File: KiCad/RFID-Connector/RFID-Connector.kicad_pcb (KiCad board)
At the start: 2 copper layers, 80 x 55.5 mm, 10 parts, among them J1 +5V power supply, J2 3V3 RX TX GND, SW1 SW_RESET_TAG_IDs, U1 ESP32-DEVKITC

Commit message: updated PCB
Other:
- board text added: "RFID-Connector PCB 1.0"
- board text removed: "RaceBox PCB 1.0"
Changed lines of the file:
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@@
   (gr_line (start 88 75.5) (end 88 20) (layer "Edge.Cuts") (width 0.1))
   (gr_circle (center 163 70.5) (end 164.5 70.5) (layer "Edge.Cuts") (width 0.1) (fill none))
-  (gr_text "RaceBox\nPCB 1.0" (at 105.45 32.725) (layer "F.SilkS")
+  (gr_text "RFID-Connector\nPCB 1.0" (at 107.95 35.56) (layer "F.SilkS")
     (effects (font (size 3 3) (thickness 0.75)))
   )

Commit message: updated pcb
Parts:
- moved J1 5.00 mm to (94.6, 50.9)
- moved J2 5.00 mm to (119.4, 66.1)
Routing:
- net Net-(J2-Pad2): track 19.9 -> 13.1 mm
- net Net-(J2-Pad3): track 19.9 -> 13.1 mm
- net Net-(J1-Pad2): track 145.8 -> 140.4 mm
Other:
- board size 80 x 55.5 mm -> 90 x 55.5 mm
- board text added: "120Ω"
- board text added: "BU"
- board text added: "RD"
- board text added: "YE"
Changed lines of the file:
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@@
   )
   (footprint "Connector_PinHeader_2.54mm:PinHeader_1x06_P2.54mm_Vertical" (layer "F.Cu")
-    (at 94.615 55.88 180)
+    (at 94.615 50.88 180)
     (descr "Through hole straight pin header, 1x06, 2.54mm pitch, single row")
     (tags "Through hole pin header THT 1x06 2.54mm single row")
@@
   )
   (footprint "Connector_PinHeader_2.54mm:PinHeader_1x04_P2.54mm_Vertical" (layer "F.Cu")
-    (at 119.38 71.12 180)
+    (at 119.38 66.12 180)
     (descr "Through hole straight pin header, 1x04, 2.54mm pitch, single row")
     (tags "Through hole pin header THT 1x04 2.54mm single row")
@@
   (gr_line (start 88.25 75.5) (end 121.25 75.5) (layer "Dwgs.User") (width 0.2))
   (gr_line (start 121.25 75.5) (end 121.25 20.5) (layer "Dwgs.User") (width 0.2))
-  (gr_circle (center 93 25) (end 94.5 25) (layer "Edge.Cuts") (width 0.1) (fill none))
-  (gr_circle (center 93 70.5) (end 94.5 70.5) (layer "Edge.Cuts") (width 0.1) (fill none))
+  (gr_circle (center 83 25) (end 84.5 25) (layer "Edge.Cuts") (width 0.1) (fill none))
+  (gr_circle (center 83 70.5) (end 84.5 70.5) (layer "Edge.Cuts") (width 0.1) (fill none))
   (gr_circle (center 163 25) (end 164.5 25) (layer "Edge.Cuts") (width 0.1) (fill none))
-  (gr_line (start 168 20) (end 88 20) (layer "Edge.Cuts") (width 0.1))
-  (gr_line (start 168 75.5) (end 88 75.5) (layer "Edge.Cuts") (width 0.1))
+  (gr_line (start 168 20) (end 78 20) (layer "Edge.Cuts") (width 0.1))
+  (gr_line (start 168 75.5) (end 78 75.5) (layer "Edge.Cuts") (width 0.1))
   (gr_line (start 168 75.5) (end 168 20) (layer "Edge.Cuts") (width 0.1))
-  (gr_line (start 88 75.5) (end 88 20) (layer "Edge.Cuts") (width 0.1))
+  (gr_line (start 78 75.5) (end 78 20) (layer "Edge.Cuts") (width 0.1))
   (gr_circle (center 163 70.5) (end 164.5 70.5) (layer "Edge.Cuts") (width 0.1) (fill none))
-  (gr_text "RFID-Connector\nPCB 1.0" (at 107.95 35.56) (layer "F.SilkS")
+  (gr_text "RFID-Connector\nPCB 1.0" (at 106.045 29.21) (layer "F.SilkS")
     (effects (font (size 3 3) (thickness 0.75)))
   )
-  (gr_text "R200" (at 105.41 59.69) (layer "F.SilkS")
+  (gr_text "RD" (at 133.35 66.04) (layer "F.SilkS")
+    (effects (font (size 1 1) (thickness 0.15)))
+  )
+  (gr_text "R200" (at 105.41 50.8) (layer "F.SilkS")
     (effects (font (size 1.8 1.8) (thickness 0.3)))
+  )
+  (gr_text "BU" (at 133.35 55.88) (layer "F.SilkS")
+    (effects (font (size 1 1) (thickness 0.15)))
   )
   (gr_text "ESP32\nDEVKIT V4" (at 146.05 71.12) (layer "F.SilkS")
     (effects (font (size 1.8 1.8) (thickness 0.3)))
+  )
+  (gr_text "YE" (at 133.35 45.72) (layer "F.SilkS")
+    (effects (font (size 1 1) (thickness 0.15)))
+  )
+  (gr_text "120Ω" (at 148.59 50.8) (layer "F.SilkS")
+    (effects (font (size 1 1) (thickness 0.15)))
   )
   (segment (start 138.43 44.45) (end 138.43 45.72) (width 1.5) (layer "B.Cu") (net 1))
@@
   (segment (start 144.78 48.26) (end 140.97 52.07) (width 1.5) (layer "B.Cu") (net 4))
   (segment (start 140.97 52.07) (end 140.97 63.5) (width 1.5) (layer "B.Cu") (net 4))
+  (segment (start 101.6 43.815) (end 101.6 45.085) (width 1.5) (layer "F.Cu") (net 6))
   (segment (start 160.02 25.4) (end 157.48 22.86) (width 1.5) (layer "F.Cu") (net 6))
-  (segment (start 99.06 53.34) (end 94.615 53.34) (width 1.5) (layer "F.Cu") (net 6))
   (segment (start 104.14 22.86) (end 101.6 25.4) (width 1.5) (layer "F.Cu") (net 6))
   (segment (start 157.48 22.86) (end 104.14 22.86) (width 1.5) (layer "F.Cu") (net 6))
-  (segment (start 101.6 25.4) (end 101.6 50.8) (width 1.5) (layer "F.Cu") (net 6))
-  (segment (start 101.6 50.8) (end 99.06 53.34) (width 1.5) (layer "F.Cu") (net 6))
+  (segment (start 101.6 25.4) (end 101.6 43.815) (width 1.5) (layer "F.Cu") (net 6))
   (segment (start 157.47 73.67) (end 160.02 71.12) (width 1.5) (layer "F.Cu") (net 6))
+  (segment (start 101.6 45.085) (end 98.345 48.34) (width 1.5) (layer "F.Cu") (net 6))
   (segment (start 160.02 71.12) (end 160.02 25.4) (width 1.5) (layer "F.Cu") (net 6))
+  (segment (start 98.345 48.34) (end 94.615 48.34) (width 1.5) (layer "F.Cu") (net 6))
   (segment (start 154.94 73.67) (end 157.47 73.67) (width 1.5) (layer "F.Cu") (net 6))
-  (segment (start 127 64.77) (end 123.19 68.58) (width 1.5) (layer "F.Cu") (net 12))
-  (segment (start 127 57.15) (end 127 64.77) (width 1.5) (layer "F.Cu") (net 12))
+  (segment (start 127 59.69) (end 123.19 63.5) (width 1.5) (layer "F.Cu") (net 12))
+  (segment (start 123.19 63.5) (end 121.08 63.5) (width 1.5) (layer "F.Cu") (net 12))
   (segment (start 129.54 55.89) (end 128.26 55.89) (width 1.5) (layer "F.Cu") (net 12))
-  (segment (start 123.19 68.58) (end 119.38 68.58) (width 1.5) (layer "F.Cu") (net 12))
   (segment (start 128.26 55.89) (end 127 57.15) (width 1.5) (layer "F.Cu") (net 12))
+  (segment (start 127 57.15) (end 127 59.69) (width 1.5) (layer "F.Cu") (net 12))
+  (segment (start 124.46 55.88) (end 124.46 58.42) (width 1.5) (layer "F.Cu") (net 13))
+  (segment (start 121.84 61.04) (end 121.08 61.04) (width 1.5) (layer "F.Cu") (net 13))
   (segment (start 129.54 53.35) (end 126.99 53.35) (width 1.5) (layer "F.Cu") (net 13))
-  (segment (start 124.46 55.88) (end 124.46 63.5) (width 1.5) (layer "F.Cu") (net 13))
-  (segment (start 124.46 63.5) (end 121.92 66.04) (width 1.5) (layer "F.Cu") (net 13))
   (segment (start 126.99 53.35) (end 124.46 55.88) (width 1.5) (layer "F.Cu") (net 13))
-  (segment (start 121.92 66.04) (end 119.38 66.04) (width 1.5) (layer "F.Cu") (net 13))
+  (segment (start 124.46 58.42) (end 121.84 61.04) (width 1.5) (layer "F.Cu") (net 13))
   (segment (start 119.38 63.5) (end 119.38 30.48) (width 1.5) (layer "F.Cu") (net 14))
   (segment (start 121.91 27.95) (end 129.54 27.95) (width 1.5) (layer "F.Cu") (net 14))

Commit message: fixed pcb
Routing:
- net Net-(J2-Pad4): track 55.2 -> 50.2 mm
- net Net-(J2-Pad2): track 13.1 -> 14.8 mm
- net Net-(J2-Pad3): track 13.1 -> 14.8 mm
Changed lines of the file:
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@@
   (segment (start 98.345 48.34) (end 94.615 48.34) (width 1.5) (layer "F.Cu") (net 6))
   (segment (start 154.94 73.67) (end 157.47 73.67) (width 1.5) (layer "F.Cu") (net 6))
-  (segment (start 127 59.69) (end 123.19 63.5) (width 1.5) (layer "F.Cu") (net 12))
-  (segment (start 123.19 63.5) (end 121.08 63.5) (width 1.5) (layer "F.Cu") (net 12))
   (segment (start 129.54 55.89) (end 128.26 55.89) (width 1.5) (layer "F.Cu") (net 12))
+  (segment (start 127 57.15) (end 127 59.69) (width 1.5) (layer "F.Cu") (net 12))
+  (segment (start 123.11 63.58) (end 119.38 63.58) (width 1.5) (layer "F.Cu") (net 12))
+  (segment (start 127 59.69) (end 123.11 63.58) (width 1.5) (layer "F.Cu") (net 12))
   (segment (start 128.26 55.89) (end 127 57.15) (width 1.5) (layer "F.Cu") (net 12))
-  (segment (start 127 57.15) (end 127 59.69) (width 1.5) (layer "F.Cu") (net 12))
+  (segment (start 121.84 61.04) (end 119.38 61.04) (width 1.5) (layer "F.Cu") (net 13))
+  (segment (start 124.46 58.42) (end 121.84 61.04) (width 1.5) (layer "F.Cu") (net 13))
   (segment (start 124.46 55.88) (end 124.46 58.42) (width 1.5) (layer "F.Cu") (net 13))
-  (segment (start 121.84 61.04) (end 121.08 61.04) (width 1.5) (layer "F.Cu") (net 13))
   (segment (start 129.54 53.35) (end 126.99 53.35) (width 1.5) (layer "F.Cu") (net 13))
   (segment (start 126.99 53.35) (end 124.46 55.88) (width 1.5) (layer "F.Cu") (net 13))
-  (segment (start 124.46 58.42) (end 121.84 61.04) (width 1.5) (layer "F.Cu") (net 13))
-  (segment (start 119.38 63.5) (end 119.38 30.48) (width 1.5) (layer "F.Cu") (net 14))
   (segment (start 121.91 27.95) (end 129.54 27.95) (width 1.5) (layer "F.Cu") (net 14))
+  (segment (start 119.38 58.5) (end 119.38 30.48) (width 1.5) (layer "F.Cu") (net 14))
   (segment (start 119.38 30.48) (end 121.91 27.95) (width 1.5) (layer "F.Cu") (net 14))
   (segment (start 133.91 28.23) (end 140.41 28.23) (width 1.5) (layer "B.Cu") (net 14))

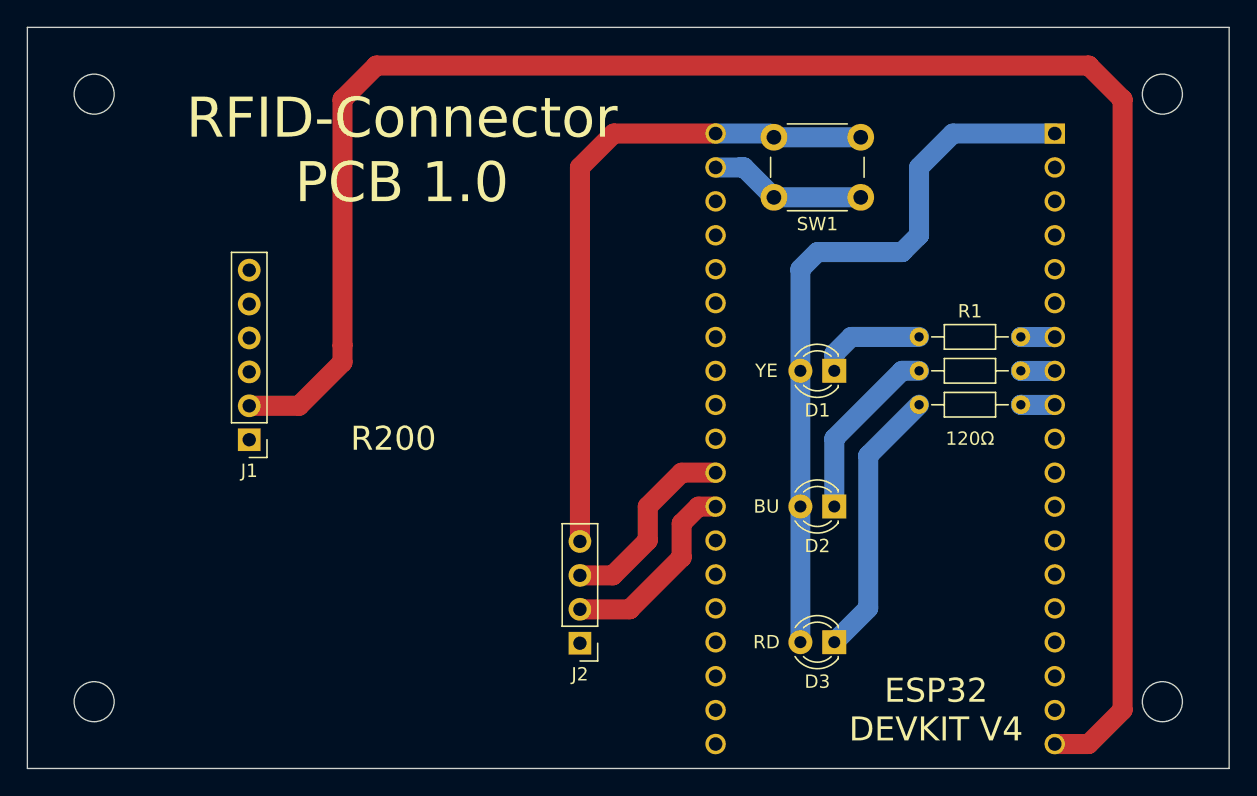
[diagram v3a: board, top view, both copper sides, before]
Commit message: added power connector to pcb
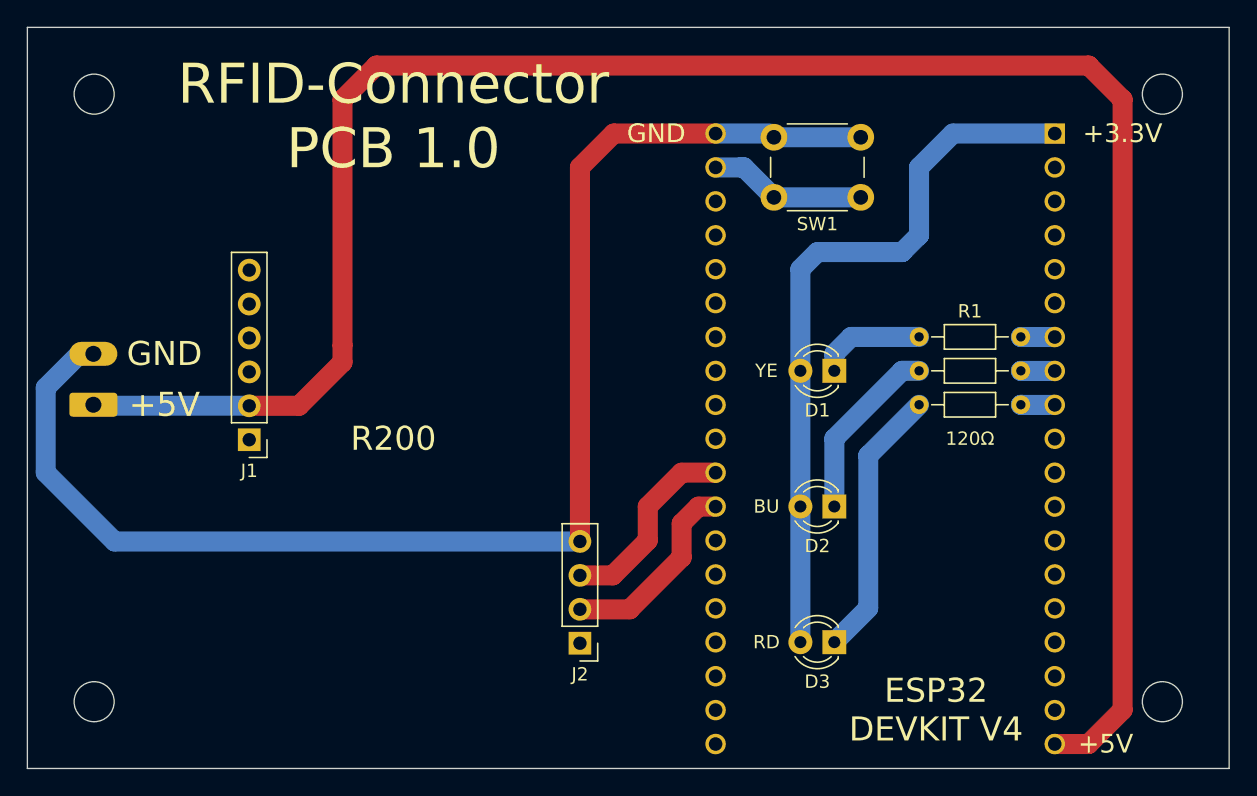
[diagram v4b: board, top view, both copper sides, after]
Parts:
- added J3: Conn_01x02, Connector_Phoenix_MC:PhoenixContact_MC_1,5_2-G-3.81_1x02_P3.81mm_Horizontal, B.Cu at (82.9, 48.3)
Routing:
- net Net-(J2-Pad4): track 50.2 -> 103.3 mm
- net Net-(J1-Pad2): track 140.4 -> 152.0 mm
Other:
- board text added: "+3.3V"
- board text added: "+5V"
- board text added: "GND"
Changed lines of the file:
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@@
     (descr "LED, diameter 3.0mm, 2 pins")
     (tags "LED diameter 3.0mm 2 pins")
-    (property "Sheetfile" "RaceBox.kicad_sch")
+    (property "Sheetfile" "RFID-Connector.kicad_sch")
     (property "Sheetname" "")
     (attr through_hole)
@@
     (descr "Resistor, Axial_DIN0204 series, Axial, Horizontal, pin pitch=7.62mm, 0.167W, length*diameter=3.6*1.6mm^2, http://cdn-reichelt.de/documents/datenblatt/B400/1_4W%23YAG.pdf")
     (tags "Resistor Axial_DIN0204 series Axial Horizontal pin pitch 7.62mm 0.167W length 3.6mm diameter 1.6mm")
-    (property "Sheetfile" "RaceBox.kicad_sch")
+    (property "Sheetfile" "RFID-Connector.kicad_sch")
     (property "Sheetname" "")
     (attr through_hole)
@@
     (descr "https://www.omron.com/ecb/products/pdf/en-b3f.pdf")
     (tags "tact sw push 6mm")
-    (property "Sheetfile" "RaceBox.kicad_sch")
+    (property "Sheetfile" "RFID-Connector.kicad_sch")
     (property "Sheetname" "")
     (attr through_hole)
@@
     (descr "LED, diameter 3.0mm, 2 pins")
     (tags "LED diameter 3.0mm 2 pins")
-    (property "Sheetfile" "RaceBox.kicad_sch")
+    (property "Sheetfile" "RFID-Connector.kicad_sch")
     (property "Sheetname" "")
     (attr through_hole)
@@
     (descr "Through hole straight pin header, 1x06, 2.54mm pitch, single row")
     (tags "Through hole pin header THT 1x06 2.54mm single row")
-    (property "Sheetfile" "RaceBox.kicad_sch")
+    (property "Sheetfile" "RFID-Connector.kicad_sch")
     (property "Sheetname" "")
     (attr through_hole)
@@
     (descr "Resistor, Axial_DIN0204 series, Axial, Horizontal, pin pitch=7.62mm, 0.167W, length*diameter=3.6*1.6mm^2, http://cdn-reichelt.de/documents/datenblatt/B400/1_4W%23YAG.pdf")
     (tags "Resistor Axial_DIN0204 series Axial Horizontal pin pitch 7.62mm 0.167W length 3.6mm diameter 1.6mm")
-    (property "Sheetfile" "RaceBox.kicad_sch")
+    (property "Sheetfile" "RFID-Connector.kicad_sch")
     (property "Sheetname" "")
     (attr through_hole)
@@
     (descr "Resistor, Axial_DIN0204 series, Axial, Horizontal, pin pitch=7.62mm, 0.167W, length*diameter=3.6*1.6mm^2, http://cdn-reichelt.de/documents/datenblatt/B400/1_4W%23YAG.pdf")
     (tags "Resistor Axial_DIN0204 series Axial Horizontal pin pitch 7.62mm 0.167W length 3.6mm diameter 1.6mm")
-    (property "Sheetfile" "RaceBox.kicad_sch")
+    (property "Sheetfile" "RFID-Connector.kicad_sch")
     (property "Sheetname" "")
     (attr through_hole)
@@
     (descr "LED, diameter 3.0mm, 2 pins")
     (tags "LED diameter 3.0mm 2 pins")
-    (property "Sheetfile" "RaceBox.kicad_sch")
+    (property "Sheetfile" "RFID-Connector.kicad_sch")
     (property "Sheetname" "")
     (attr through_hole)
@@
     (descr "Through hole straight pin header, 1x04, 2.54mm pitch, single row")
     (tags "Through hole pin header THT 1x04 2.54mm single row")
-    (property "Sheetfile" "RaceBox.kicad_sch")
+    (property "Sheetfile" "RFID-Connector.kicad_sch")
     (property "Sheetname" "")
     (attr through_hole)
@@
     (property "Price" "None")
     (property "STANDARD" "Manufacturer Recommendations")
-    (property "Sheetfile" "RaceBox.kicad_sch")
+    (property "Sheetfile" "RFID-Connector.kicad_sch")
     (property "Sheetname" "")
     (property "SnapEDA_Link" "https://www.snapeda.com/parts/ESP32-DEVKITC/Espressif+Systems/view-part/?ref=snap")
@@
       (net 14 "Net-(J2-Pad4)") (pinfunction "GND3") (pintype "power_in") (solder_mask_margin 0.102))
   )
+  (footprint "Connector_Phoenix_MC:PhoenixContact_MC_1,5_2-G-3.81_1x02_P3.81mm_Horizontal" (layer "B.Cu")
+    (at 82.9425 48.26 90)
+    (descr "Generic Phoenix Contact connector footprint for: MC_1,5/2-G-3.81; number of pins: 02; pin pitch: 3.81mm; Angled || order number: 1803277 8A 160V")
+    (tags "phoenix_contact connector MC_01x02_G_3.81mm")
+    (property "Sheetfile" "RFID-Connector.kicad_sch")
+    (property "Sheetname" "")
+    (attr through_hole)
+    (fp_text reference "J3" (at 1.9 3 90) (layer "B.SilkS")
+      (effects (font (size 1 1) (thickness 0.15)) (justify mirror))
+    )
+    (fp_text value "Conn_01x02" (at 1.9 -9.2 90) (layer "B.Fab")
+      (effects (font (size 1 1) (thickness 0.15)) (justify mirror))
+    )
+    (fp_text user "${REFERENCE}" (at 1.9 0.5 90) (layer "B.Fab")
+      (effects (font (size 1 1) (thickness 0.15)) (justify mirror))
+    )
+    (fp_line (start 0 2) (end -0.3 2.6) (layer "B.SilkS") (width 0.12))
+    (fp_line (start 0.3 2.6) (end 0 2) (layer "B.SilkS") (width 0.12))
+    (fp_line (start -2.71 -4.8) (end 6.52 -4.8) (layer "B.SilkS") (width 0.12))
+    (fp_line (start -2.71 1.31) (end -2.71 -8.11) (layer "B.SilkS") (width 0.12))
+    (fp_line (start 6.52 1.31) (end 4.86 1.31) (layer "B.SilkS") (width 0.12))
+    (fp_line (start 1.05 1.31) (end 2.76 1.31) (layer "B.SilkS") (width 0.12))
+    (fp_line (start 6.52 -8.11) (end 6.52 1.31) (layer "B.SilkS") (width 0.12))
+    (fp_line (start -2.71 1.31) (end -1.05 1.31) (layer "B.SilkS") (width 0.12))
+    (fp_line (start -2.71 -8.11) (end 6.52 -8.11) (layer "B.SilkS") (width 0.12))
+    (fp_line (start -0.3 2.6) (end 0.3 2.6) (layer "B.SilkS") (width 0.12))
+    (fp_line (start -3.21 -8.5) (end 6.91 -8.5) (layer "B.CrtYd") (width 0.05))
+    (fp_line (start -3.21 2.3) (end -3.21 -8.5) (layer "B.CrtYd") (width 0.05))
+    (fp_line (start 6.91 -8.5) (end 6.91 2.3) (layer "B.CrtYd") (width 0.05))
+    (fp_line (start 6.91 2.3) (end -3.21 2.3) (layer "B.CrtYd") (width 0.05))
+    (fp_line (start 6.41 -8) (end 6.41 1.2) (layer "B.Fab") (width 0.1))
+    (fp_line (start 0 0) (end -0.8 1.2) (layer "B.Fab") (width 0.1))
+    (fp_line (start 0.8 1.2) (end 0 0) (layer "B.Fab") (width 0.1))
+    (fp_line (start -2.6 -8) (end 6.41 -8) (layer "B.Fab") (width 0.1))
+    (fp_line (start -2.6 1.2) (end -2.6 -8) (layer "B.Fab") (width 0.1))
+    (fp_line (start 6.41 1.2) (end -2.6 1.2) (layer "B.Fab") (width 0.1))
+    (pad "1" thru_hole roundrect (at 0 0 90) (size 1.8 3.6) (drill 1.2) (layers *.Cu *.Mask) (roundrect_rratio 0.138889)
+      (net 6 "Net-(J1-Pad2)") (pinfunction "Pin_1") (pintype "passive"))
+    (pad "2" thru_hole oval (at 3.81 0 90) (size 1.8 3.6) (drill 1.2) (layers *.Cu *.Mask)
+      (net 14 "Net-(J2-Pad4)") (pinfunction "Pin_2") (pintype "passive"))
+    (model "${KICAD6_3DMODEL_DIR}/Connector_Phoenix_MC.3dshapes/PhoenixContact_MC_1,5_2-G-3.81_1x02_P3.81mm_Horizontal.wrl"
+      (offset (xyz 0 0 0))
+      (scale (xyz 1 1 1))
+      (rotate (xyz 0 0 0))
+    )
+  )
   (gr_line (start 88.25 20.5) (end 121.25 20.5) (layer "Dwgs.User") (width 0.2))
   (gr_line (start 88.25 20.5) (end 88.25 75.5) (layer "Dwgs.User") (width 0.2))
@@
   (gr_line (start 78 75.5) (end 78 20) (layer "Edge.Cuts") (width 0.1))
   (gr_circle (center 163 70.5) (end 164.5 70.5) (layer "Edge.Cuts") (width 0.1) (fill none))
-  (gr_text "RFID-Connector\nPCB 1.0" (at 106.045 29.21) (layer "F.SilkS")
+  (gr_text "+5V" (at 88.265 48.26) (layer "B.SilkS")
+    (effects (font (size 1.8 1.8) (thickness 0.3)) (justify mirror))
+  )
+  (gr_text "GND" (at 88.265 44.45) (layer "B.SilkS")
+    (effects (font (size 1.8 1.8) (thickness 0.3)) (justify mirror))
+  )
+  (gr_text "RFID-Connector\nPCB 1.0" (at 105.41 26.67) (layer "F.SilkS")
     (effects (font (size 3 3) (thickness 0.75)))
+  )
+  (gr_text "+5V" (at 88.265 48.26) (layer "F.SilkS")
+    (effects (font (size 1.8 1.8) (thickness 0.3)))
   )
   (gr_text "RD" (at 133.35 66.04) (layer "F.SilkS")
@@
     (effects (font (size 1.8 1.8) (thickness 0.3)))
   )
+  (gr_text "GND" (at 88.265 44.45) (layer "F.SilkS")
+    (effects (font (size 1.8 1.8) (thickness 0.3)))
+  )
   (gr_text "BU" (at 133.35 55.88) (layer "F.SilkS")
     (effects (font (size 1 1) (thickness 0.15)))
@@
     (effects (font (size 1 1) (thickness 0.15)))
   )
+  (gr_text "GND" (at 125.095 27.94) (layer "F.SilkS")
+    (effects (font (size 1.4 1.4) (thickness 0.3)))
+  )
   (gr_text "120Ω" (at 148.59 50.8) (layer "F.SilkS")
     (effects (font (size 1 1) (thickness 0.15)))
+  )
+  (gr_text "+3.3V" (at 160.02 27.94) (layer "F.SilkS")
+    (effects (font (size 1.4 1.4) (thickness 0.3)))
+  )
+  (gr_text "+5V" (at 158.75 73.66) (layer "F.SilkS")
+    (effects (font (size 1.4 1.4) (thickness 0.3)))
   )
   (segment (start 138.43 44.45) (end 138.43 45.72) (width 1.5) (layer "B.Cu") (net 1))
@@
   (segment (start 98.345 48.34) (end 94.615 48.34) (width 1.5) (layer "F.Cu") (net 6))
   (segment (start 154.94 73.67) (end 157.47 73.67) (width 1.5) (layer "F.Cu") (net 6))
+  (segment (start 94.615 48.34) (end 83.0225 48.34) (width 1.5) (layer "B.Cu") (net 6))
   (segment (start 129.54 55.89) (end 128.26 55.89) (width 1.5) (layer "F.Cu") (net 12))
   (segment (start 127 57.15) (end 127 59.69) (width 1.5) (layer "F.Cu") (net 12))
@@
   (segment (start 119.38 58.5) (end 119.38 30.48) (width 1.5) (layer "F.Cu") (net 14))
   (segment (start 119.38 30.48) (end 121.91 27.95) (width 1.5) (layer "F.Cu") (net 14))
+  (segment (start 79.375 46.99) (end 81.915 44.45) (width 1.5) (layer "B.Cu") (net 14))
   (segment (start 133.91 28.23) (end 140.41 28.23) (width 1.5) (layer "B.Cu") (net 14))
+  (segment (start 119.38 58.5) (end 84.535 58.5) (width 1.5) (layer "B.Cu") (net 14))
   (segment (start 133.63 27.95) (end 133.91 28.23) (width 0.25) (layer "B.Cu") (net 14))
   (segment (start 129.54 27.95) (end 133.63 27.95) (width 1.5) (layer "B.Cu") (net 14))
+  (segment (start 84.535 58.5) (end 79.375 53.34) (width 1.5) (layer "B.Cu") (net 14))
+  (segment (start 79.375 53.34) (end 79.375 46.99) (width 1.5) (layer "B.Cu") (net 14))
+  (segment (start 81.915 44.45) (end 82.9425 44.45) (width 1.5) (layer "B.Cu") (net 14))
   (segment (start 152.41 43.19) (end 152.4 43.18) (width 1.5) (layer "B.Cu") (net 15))
   (segment (start 154.94 43.19) (end 152.41 43.19) (width 1.5) (layer "B.Cu") (net 15))
